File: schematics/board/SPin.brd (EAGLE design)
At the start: 70 x 70 mm, 15 parts

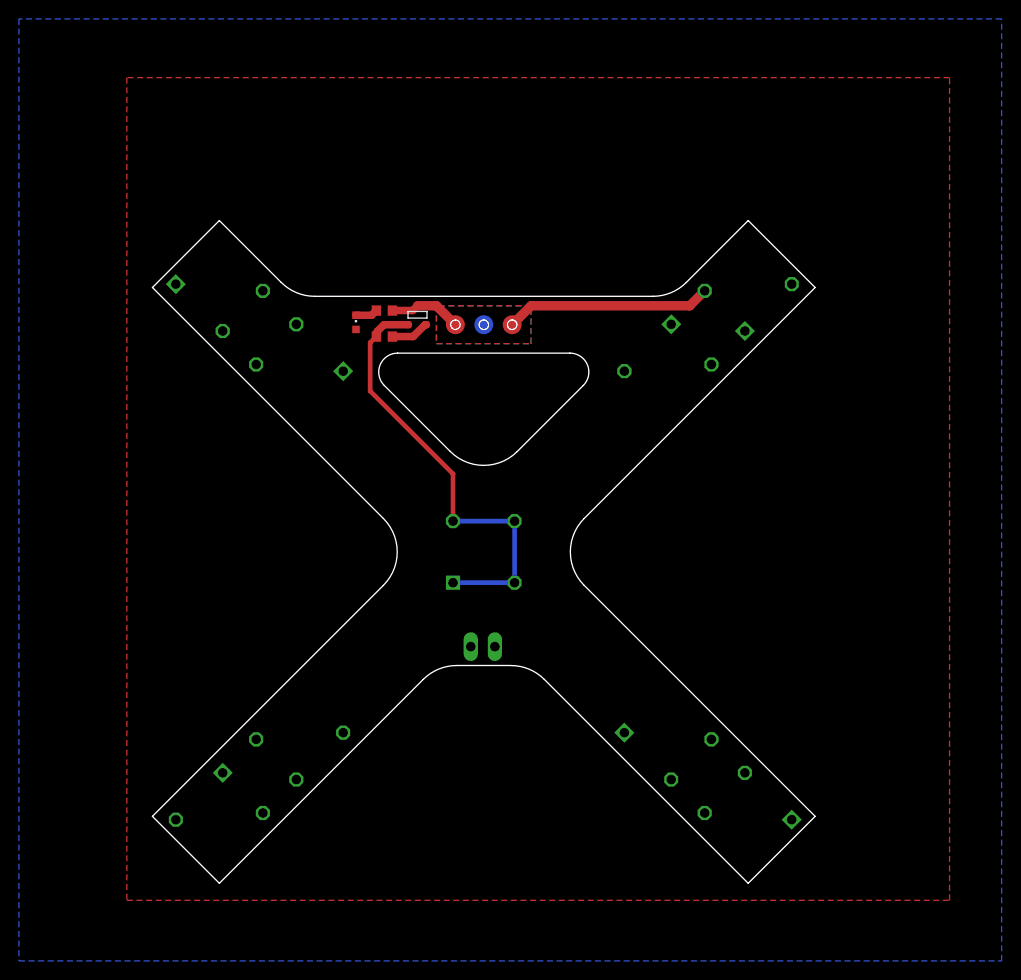
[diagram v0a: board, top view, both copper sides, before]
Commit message: Добавлена схема дозиметра, исправлены платы СБ
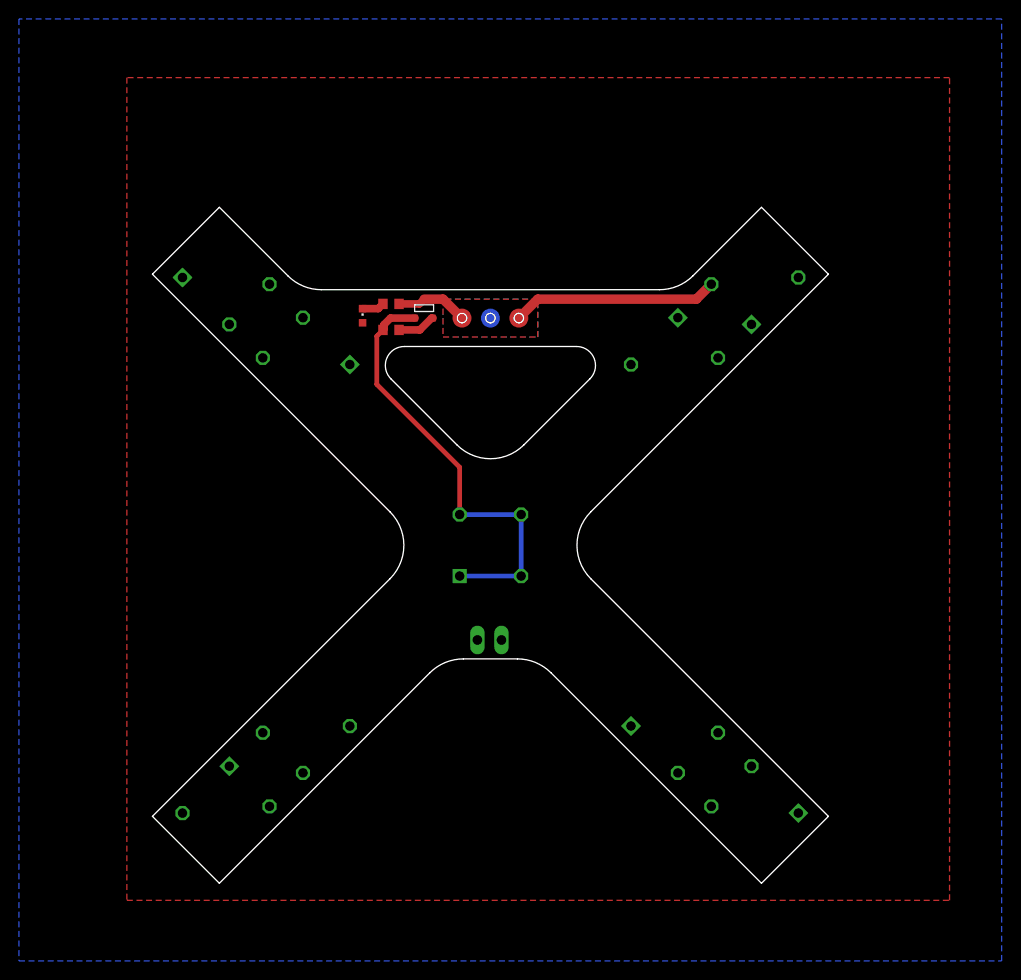
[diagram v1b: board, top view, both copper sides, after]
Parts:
- moved U$3 0.99 mm to (63.6, 63.6)
- moved U$1 0.99 mm to (7.77, 63.6)
- moved U$20 0.99 mm to (63.6, 7.77)
- moved U$19 0.99 mm to (16.3, 16.3)
- moved JP1 0.99 mm to (35.6, 25.7)
- moved LED7 0.99 mm to (22.2, 60.0)
- moved R13 0.99 mm to (25.2, 61.2)
- moved R14 0.99 mm to (25.2, 58.5)
- moved U$13 0.99 mm to (28.7, 60.7)
- moved U$18 0.99 mm to (7.77, 7.77)
- moved U$6 0.99 mm to (35.7, 59.7)
- moved U$2 0.99 mm to (16.3, 55.1)
- moved U$21 0.99 mm to (55.1, 16.3)
- moved U$4 0.99 mm to (55.1, 55.1)
- moved U$5 0.99 mm to (35.7, 35.7)
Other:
- board size 70 x 70 mm -> 71.4 x 71.4 mm

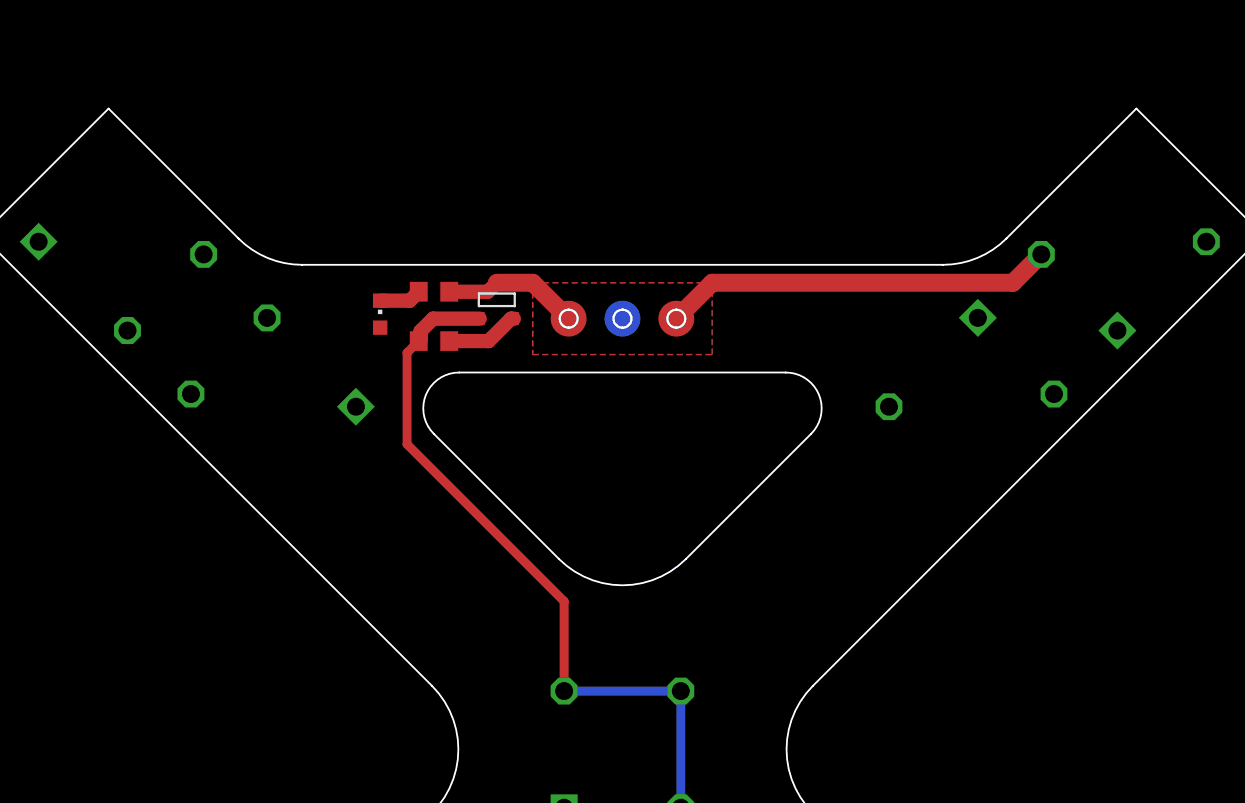
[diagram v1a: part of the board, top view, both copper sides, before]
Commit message: Плата СП изменена для возможности подключения 2 вариантов ФЭПов
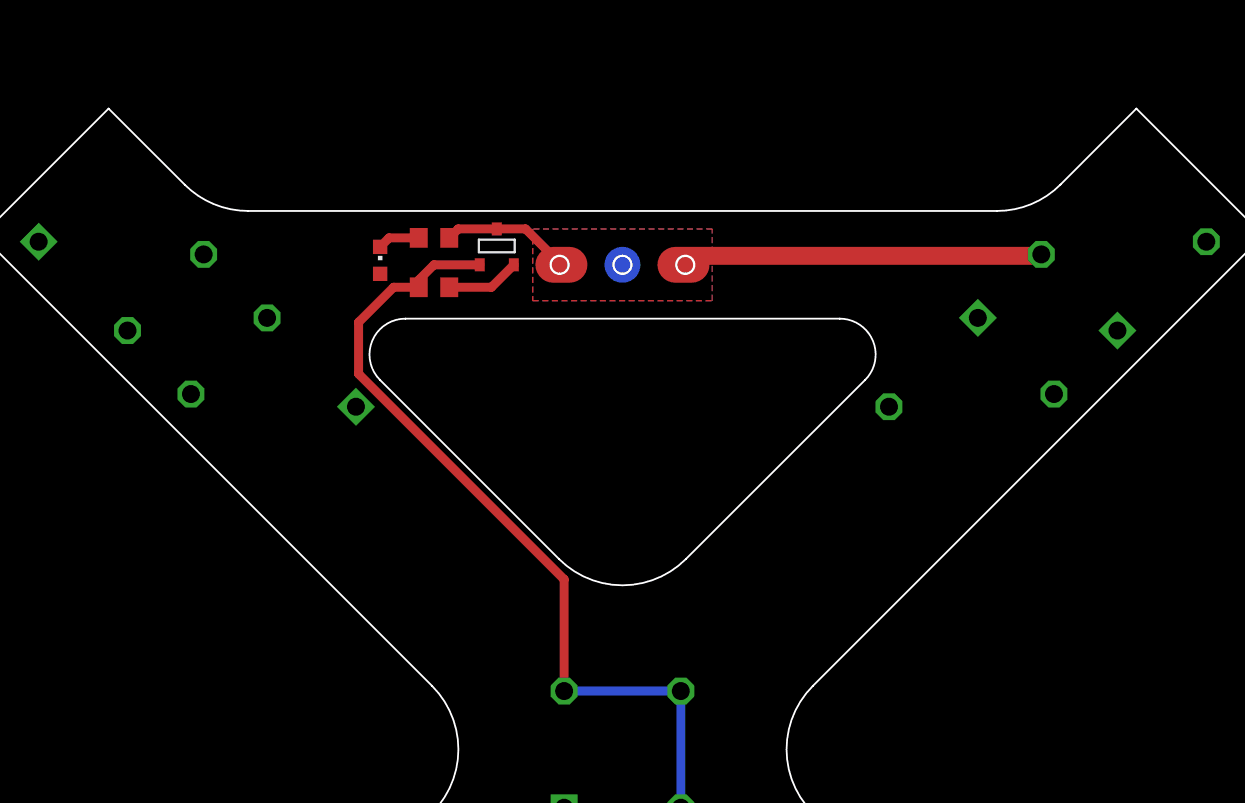
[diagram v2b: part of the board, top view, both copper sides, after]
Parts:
- U$6: value GRAFITGRAFIT3_1 -> GRAFITGRAFIT4_2; device CanCubeSat:GRAFIT3_1 -> CanCubeSat:GRAFIT4_2
- moved U$6 3.00 mm to (35.7, 62.7)
- moved LED7 3.00 mm to (22.2, 63.0)
- moved R13 3.00 mm to (25.2, 64.2)
- moved R14 3.00 mm to (25.2, 61.5)
- moved U$13 3.00 mm to (28.7, 63.7)
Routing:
- net ROZE: track 47.1 -> 53.1 mm
- net BUS+: track 21.8 -> 20.2 mm
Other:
- outline, holes or cut-outs redrawn
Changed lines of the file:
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@@
 <setting verticaltext="up"/>
 </settings>
-<grid distance="0.7" unitdist="mm" unit="mm" style="lines" multiple="1" display="yes" altdistance="0.25" altunitdist="mm" altunit="mm"/>
+<grid distance="0.5" unitdist="mm" unit="mm" style="lines" multiple="1" display="yes" altdistance="0.25" altunitdist="mm" altunit="mm"/>
 <layers>
 <layer number="1" name="Top" color="4" fill="1" visible="yes" active="yes"/>
@@
 <wire x1="46.308" y1="32.166" x2="46.308" y2="39.237" width="0.1" layer="20" curve="-90"/>
 <wire x1="71.404" y1="64.333" x2="46.308" y2="39.237" width="0.1" layer="20"/>
-<wire x1="26.6031" y1="56.7" x2="44.800571875" y2="56.7" width="0.1" layer="20"/>
-<wire x1="44.800571875" y1="56.7" x2="46.2147875" y2="53.2857875" width="0.1" layer="20" curve="-134.999937"/>
-<wire x1="46.2147875" y1="53.2857875" x2="39.237" y2="46.308" width="0.1" layer="20"/>
-<wire x1="17.84606875" y1="62.7" x2="53.55793125" y2="62.7" width="0.1" layer="20"/>
-<wire x1="53.55793125" y1="62.7" x2="57.093465625" y2="64.164465625" width="0.1" layer="20" curve="45"/>
-<wire x1="57.093465625" y1="64.164465625" x2="64.333" y2="71.404" width="0.1" layer="20"/>
+<wire x1="32.166" y1="46.308" x2="22.192365625" y2="56.28610625" width="0.1" layer="20"/>
+<wire x1="22.192365625" y1="56.28610625" x2="23.606896875" y2="59.7" width="0.1" layer="20" curve="-134.987149"/>
+<wire x1="23.606896875" y1="59.7" x2="47.807278125" y2="59.7" width="0.1" layer="20"/>
+<wire x1="47.807278125" y1="59.7" x2="49.221015625" y2="56.285309375" width="0.1" layer="20" curve="-135.019308"/>
+<wire x1="49.221015625" y1="56.285309375" x2="39.237" y2="46.308" width="0.1" layer="20"/>
+<wire x1="7.071" y1="71.404" x2="11.3158" y2="67.16291875" width="0.1" layer="20"/>
+<wire x1="11.3158" y1="67.16291875" x2="14.849784375" y2="65.7" width="0.1" layer="20" curve="44.974906"/>
+<wire x1="14.849784375" y1="65.7" x2="56.56461875" y2="65.7" width="0.1" layer="20"/>
+<wire x1="56.56461875" y1="65.7" x2="60.10294375" y2="67.167259375" width="0.1" layer="20" curve="45.045249"/>
+<wire x1="60.10294375" y1="67.167259375" x2="64.333" y2="71.404" width="0.1" layer="20"/>
 <wire x1="0" y1="64.333" x2="25.095" y2="39.237" width="0.1" layer="20"/>
-<wire x1="32.166" y1="46.308" x2="25.188815625" y2="53.28585625" width="0.1" layer="20"/>
-<wire x1="25.188815625" y1="53.28585625" x2="26.6031" y2="56.7" width="0.1" layer="20" curve="-134.997304"/>
 <wire x1="64.333" y1="71.404" x2="71.404" y2="64.333" width="0.1" layer="20"/>
 <wire x1="39.237" y1="46.308" x2="32.166" y2="46.308" width="0.1" layer="20" curve="-90"/>
-<wire x1="7.071" y1="71.404" x2="14.310534375" y2="64.164465625" width="0.1" layer="20"/>
-<wire x1="14.310534375" y1="64.164465625" x2="17.84606875" y2="62.7" width="0.1" layer="20" curve="45"/>
 <wire x1="0" y1="64.333" x2="7.071" y2="71.404" width="0.1" layer="20"/>
 </plain>
@@
 <attribute name="VALUE" x="33.06000625" y="28.875003125" size="1.27" layer="28" rot="MR180"/>
 </element>
-<element name="U$13" library="CanCubeSat" package="SOT23-3" value="SI2302CDS" x="28.7" y="60.7" smashed="yes"/>
-<element name="R13" library="resistor" package="R0603" package3d_urn="urn:adsk.eagle:package:23555/3" value="1k5" x="25.2" y="61.2" smashed="yes">
-<attribute name="VALUE" x="24.565" y="59.295" size="1.27" layer="27"/>
-</element>
-<element name="LED7" library="led" library_urn="urn:adsk.eagle:library:259" package="CHIPLED_0603" package3d_urn="urn:adsk.eagle:package:15822/2" value="" x="22.2" y="59.95" smashed="yes">
-<attribute name="POPULARITY" value="28" x="10.2" y="69.95" size="1.778" layer="27" display="off"/>
-<attribute name="VALUE" x="24.105" y="58.68" size="1.27" layer="27" rot="R90"/>
-</element>
-<element name="R14" library="resistor" package="R0603" package3d_urn="urn:adsk.eagle:package:23555/3" value="1M" x="25.2" y="58.45" smashed="yes">
-<attribute name="VALUE" x="24.565" y="56.545" size="1.27" layer="27"/>
-</element>
-<element name="U$6" library="CanCubeSat" package="GRAFIT3_1" value="GRAFITGRAFIT3_1" x="35.702" y="59.7" smashed="yes" rot="R90"/>
+<element name="U$13" library="CanCubeSat" package="SOT23-3" value="SI2302CDS" x="28.7" y="63.7" smashed="yes"/>
+<element name="R13" library="resistor" package="R0603" package3d_urn="urn:adsk.eagle:package:23555/3" value="1k5" x="25.2" y="64.2" smashed="yes">
+<attribute name="VALUE" x="24.565" y="62.295" size="1.27" layer="27"/>
+</element>
+<element name="LED7" library="led" library_urn="urn:adsk.eagle:library:259" package="CHIPLED_0603" package3d_urn="urn:adsk.eagle:package:15822/2" value="" x="22.2" y="62.95" smashed="yes">
+<attribute name="POPULARITY" value="28" x="10.2" y="72.95" size="1.778" layer="27" display="off"/>
+<attribute name="VALUE" x="24.105" y="61.68" size="1.27" layer="27" rot="R90"/>
+</element>
+<element name="R14" library="resistor" package="R0603" package3d_urn="urn:adsk.eagle:package:23555/3" value="1M" x="25.2" y="61.45" smashed="yes">
+<attribute name="VALUE" x="24.565" y="59.545" size="1.27" layer="27"/>
+</element>
+<element name="U$6" library="CanCubeSat" package="GRAFIT4_2" value="GRAFITGRAFIT4_2" x="35.7" y="62.7" smashed="yes" rot="R90"/>
 <element name="U$5" library="CanCubeSat" package="KCONNECT-_QUAD" value="KCONNECTQUAD-" x="35.702" y="35.702" smashed="yes">
 <attribute name="VALUE" x="32.162" y="29.257" size="1.27" layer="27"/>
@@
 <contactref element="LED7" pad="A"/>
 <contactref element="U$6" pad="P$2"/>
-<wire x1="38.702" y1="59.7" x2="40.702" y2="61.7" width="1" layer="1"/>
-<wire x1="57.4573625" y1="61.7" x2="59.03680625" y2="63.27944375" width="1" layer="1"/>
-<wire x1="40.702" y1="61.7" x2="57.4573625" y2="61.7" width="1" layer="1"/>
+<wire x1="58.9573625" y1="63.2" x2="59.03680625" y2="63.27944375" width="1" layer="1"/>
+<wire x1="39.1" y1="62.7" x2="39.6" y2="63.2" width="1" layer="1"/>
+<wire x1="58.9573625" y1="63.2" x2="39.6" y2="63.2" width="1" layer="1"/>
 <polygon width="0.1" layer="1" pour="cutout">
-<vertex x="30.7" y="61.7"/>
-<vertex x="30.7" y="57.7"/>
-<vertex x="40.7" y="57.7"/>
-<vertex x="40.7" y="61.7"/>
+<vertex x="30.7" y="64.7"/>
+<vertex x="30.7" y="60.7"/>
+<vertex x="40.7" y="60.7"/>
+<vertex x="40.7" y="64.7"/>
 </polygon>
 </signal>
@@
 </polygon>
 <polygon width="0.1" layer="16" pour="cutout">
-<vertex x="30.7" y="61.7"/>
-<vertex x="30.7" y="57.7"/>
-<vertex x="40.7" y="57.7"/>
-<vertex x="40.7" y="61.7"/>
+<vertex x="30.7" y="64.7"/>
+<vertex x="30.7" y="60.7"/>
+<vertex x="40.7" y="60.7"/>
+<vertex x="40.7" y="64.7"/>
 </polygon>
 </signal>
@@
 <contactref element="U$13" pad="2"/>
 <contactref element="R14" pad="2"/>
-<wire x1="29.49353125" y1="59.7" x2="29.65" y2="59.7" width="0.8" layer="1"/>
-<wire x1="28.24353125" y1="58.45" x2="26.05" y2="58.45" width="0.8" layer="1"/>
-<wire x1="28.24353125" y1="58.45" x2="29.49353125" y2="59.7" width="0.8" layer="1"/>
+<wire x1="26.05" y1="61.45" x2="28.4" y2="61.45" width="0.5" layer="1"/>
+<wire x1="28.4" y1="61.45" x2="29.65" y2="62.7" width="0.5" layer="1"/>
 </signal>
 <signal name="ROZE">
@@
 <contactref element="U$13" pad="1"/>
 <contactref element="U$5" pad="1"/>
-<wire x1="27.75" y1="59.7" x2="25.15146875" y2="59.7" width="0.8" layer="1"/>
-<wire x1="25.15146875" y1="59.7" x2="24.45" y2="58.99853125" width="0.8" layer="1"/>
-<wire x1="24.45" y1="58.99853125" x2="24.45" y2="58.55" width="0.8" layer="1"/>
-<wire x1="24.45" y1="58.55" x2="24.35" y2="58.45" width="0.8" layer="1"/>
 <contactref element="U$5" pad="2"/>
 <contactref element="U$5" pad="3"/>
 <contactref element="U$5" pad="4"/>
-<wire x1="32.452" y1="38.952" x2="32.452" y2="43.948" width="0.5" layer="1"/>
-<wire x1="23.7" y1="57.8" x2="24.35" y2="58.45" width="0.5" layer="1"/>
-<wire x1="32.452" y1="43.948" x2="23.7" y2="52.7" width="0.5" layer="1"/>
-<wire x1="23.7" y1="52.7" x2="23.7" y2="57.8" width="0.5" layer="1"/>
 <wire x1="32.452" y1="38.952" x2="38.952" y2="38.952" width="0.5" layer="16"/>
 <wire x1="38.952" y1="38.952" x2="38.952" y2="32.452" width="0.5" layer="16"/>
 <wire x1="38.952" y1="32.452" x2="32.452" y2="32.452" width="0.5" layer="16"/>
+<wire x1="32.452" y1="45.17339375" x2="21" y2="56.62539375" width="0.5" layer="1"/>
+<wire x1="21" y1="56.62539375" x2="21" y2="59.5" width="0.5" layer="1"/>
+<wire x1="21" y1="59.5" x2="22.95" y2="61.45" width="0.5" layer="1"/>
+<wire x1="22.95" y1="61.45" x2="24.35" y2="61.45" width="0.5" layer="1"/>
+<wire x1="32.452" y1="38.952" x2="32.452" y2="45.17339375" width="0.5" layer="1"/>
+<wire x1="27.75" y1="62.7" x2="25.2" y2="62.7" width="0.5" layer="1"/>
+<wire x1="24.35" y1="61.85" x2="24.35" y2="61.45" width="0.5" layer="1"/>
+<wire x1="25.2" y1="62.7" x2="24.35" y2="61.85" width="0.5" layer="1"/>
 </signal>
 <signal name="N$29">
 <contactref element="LED7" pad="C"/>
 <contactref element="R13" pad="1"/>
-<wire x1="24.35" y1="61.2" x2="23.85" y2="60.7" width="0.8" layer="1"/>
-<wire x1="23.85" y1="60.7" x2="22.2" y2="60.7" width="0.8" layer="1"/>
+<wire x1="22.2" y1="63.7" x2="22.7" y2="64.2" width="0.5" layer="1"/>
+<wire x1="22.7" y1="64.2" x2="24.35" y2="64.2" width="0.5" layer="1"/>
 </signal>
 <signal name="2">
@@
 <contactref element="R13" pad="2"/>
 <contactref element="U$6" pad="P$1"/>
-<wire x1="28.7" y1="61.7" x2="28.2" y2="61.2" width="0.8" layer="1"/>
-<wire x1="28.2" y1="61.2" x2="26.05" y2="61.2" width="0.8" layer="1"/>
-<wire x1="32.702" y1="59.7" x2="30.702" y2="61.7" width="1" layer="1"/>
-<wire x1="30.702" y1="61.7" x2="28.7" y2="61.7" width="1" layer="1"/>
+<wire x1="26.05" y1="64.2" x2="26.55" y2="64.7" width="0.5" layer="1"/>
+<wire x1="26.55" y1="64.7" x2="28.7" y2="64.7" width="0.5" layer="1"/>
+<wire x1="32.3" y1="62.7" x2="30.3" y2="64.7" width="0.5" layer="1"/>
+<wire x1="30.3" y1="64.7" x2="28.7" y2="64.7" width="0.5" layer="1"/>
 </signal>
 </signals>
